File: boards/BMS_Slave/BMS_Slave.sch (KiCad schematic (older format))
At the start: 63 parts, among them J1 Mounting_Hole_4-40, J2 Mounting_Hole_4-40, J3 Mounting_Hole_4-40, J4 Mounting_Hole_4-40, J5 MicroFit_12, J6 MicroFit_20, J7 NanoFit_2, J8 NanoFit_2, Q1 Q_NPN_BCE, T1 T_LAN_7490100111A, U1 LTC6811-1, U2 24AA01, U3 MCP6001, U4 LTC1380, U5 LTC1380, U6 MCP6001

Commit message: Revert "testing"
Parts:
- J2, J4: footprint footprints:Mounting_Hole_Insert_4-40 -> footprints:Mounting_Hole_4-40
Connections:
- net CELL_TEMP1: now also J6.6; no longer J6.11
- net CELL_TEMP10: now also J6.16; no longer J6.20
- net CELL_TEMP2: now also J6.7; no longer J6.12
- net CELL_TEMP3: now also J6.8; no longer J6.13
- net CELL_TEMP4: now also J6.9; no longer J6.14
- net CELL_TEMP5: now also J6.10; no longer J6.15
- net CELL_TEMP6: now also J6.20; no longer J6.16
- net CELL_TEMP7: now also J6.19; no longer J6.17
- net CELL_TEMP9: now also J6.17; no longer J6.19
- net GND: now also J6.11, J6.12, J6.13, J6.14, J6.15; no longer J6.10, J6.6, J6.7, J6.8, J6.9
- net VREG: no longer U1.40 (ISOMD)
- net Cell1: no longer names the net of F10.1, J5.8
- net Cell10: no longer names the net of F1.1, J5.6
- net Cell2: no longer names the net of F9.1, J5.1
- net Cell3: no longer names the net of F8.1, J5.2
- net Cell4: no longer names the net of F7.1, J5.3
- net Cell5: no longer names the net of F6.1, J5.9
- net Cell6: no longer names the net of F5.1, J5.10
- net Cell7: no longer names the net of F4.1, J5.11
- net Cell8: no longer names the net of F3.1, J5.5
- net Cell9: no longer names the net of F2.1, J5.12
- net LowSide: no longer names the net of F11.1, J5.7
- net LowSide: no longer J5.4
- no-connect marks 15 -> 17
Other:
- moved on the sheet: J6

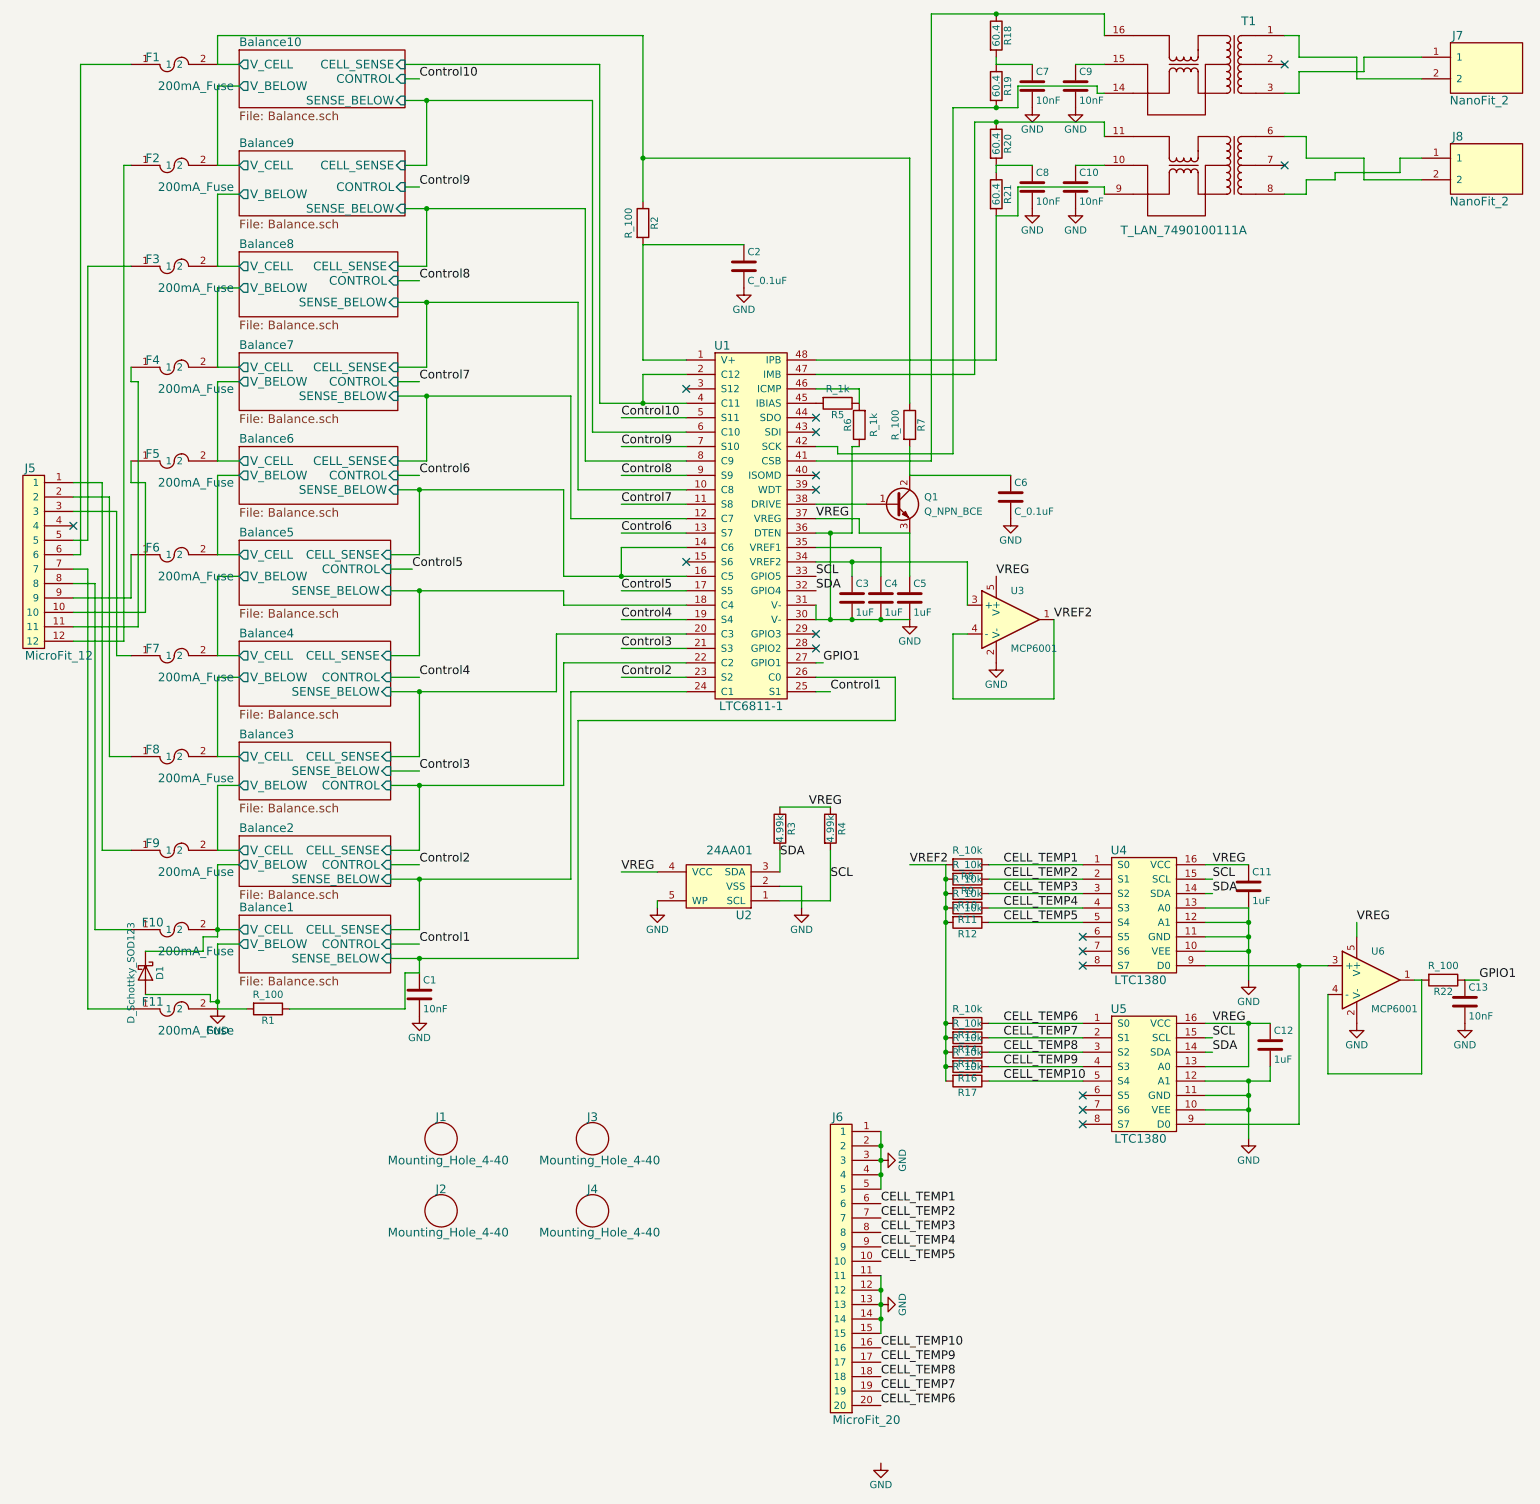
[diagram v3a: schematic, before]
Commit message: BMS Slave: Changed orientation of connectors
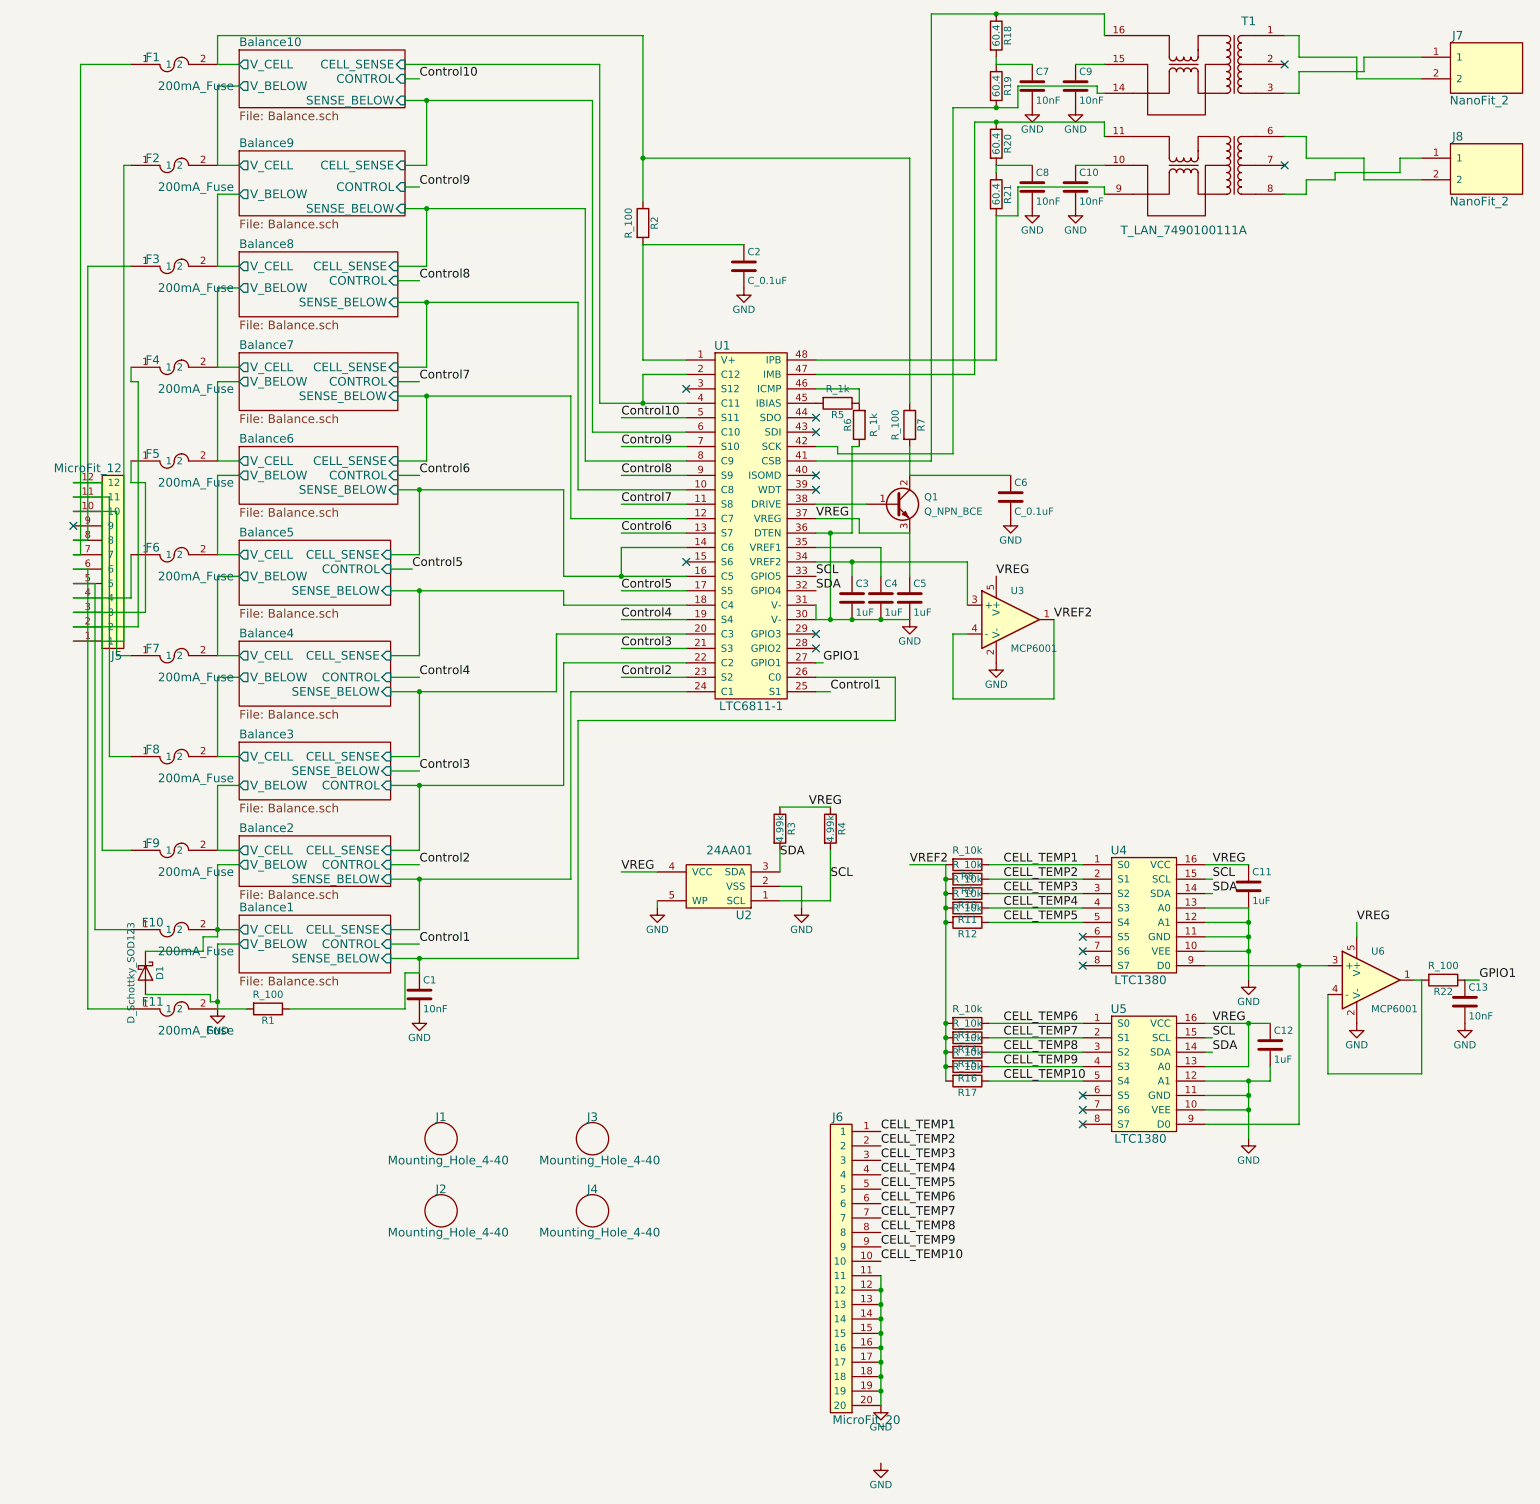
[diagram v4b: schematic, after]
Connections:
- net CELL_TEMP1: now also J6.1; no longer J6.6
- net CELL_TEMP10: now also J6.10; no longer J6.16
- net CELL_TEMP2: now also J6.2; no longer J6.7
- net CELL_TEMP3: now also J6.3; no longer J6.8
- net CELL_TEMP4: now also J6.4; no longer J6.9
- net CELL_TEMP5: now also J6.5; no longer J6.10
- net CELL_TEMP6: now also J6.6; no longer J6.20
- net CELL_TEMP7: now also J6.7; no longer J6.19
- net CELL_TEMP8: now also J6.8; no longer J6.18
- net CELL_TEMP9: now also J6.9; no longer J6.17
- net GND: now also J6.16, J6.17, J6.18, J6.19, J6.20; no longer J6.1, J6.2, J6.3, J6.4, J6.5
- net at F1.1: now also J5.7; no longer J5.6
- net at F2.1: now also J5.1; no longer J5.12
- net at F3.1: now also J5.8; no longer J5.5
- net at F4.1: now also J5.2; no longer J5.11
- net at F5.1: now also J5.3; no longer J5.10
- net at F6.1: now also J5.4; no longer J5.9
- net at F7.1: now also J5.10; no longer J5.3
- net at F8.1: now also J5.11; no longer J5.2
- net at F9.1: now also J5.12; no longer J5.1
- net at F10.1: now also J5.5; no longer J5.8
- net at F11.1: now also J5.6; no longer J5.7
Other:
- moved on the sheet: J5

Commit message: BMS Slave: Added CAD and updated Gerbers
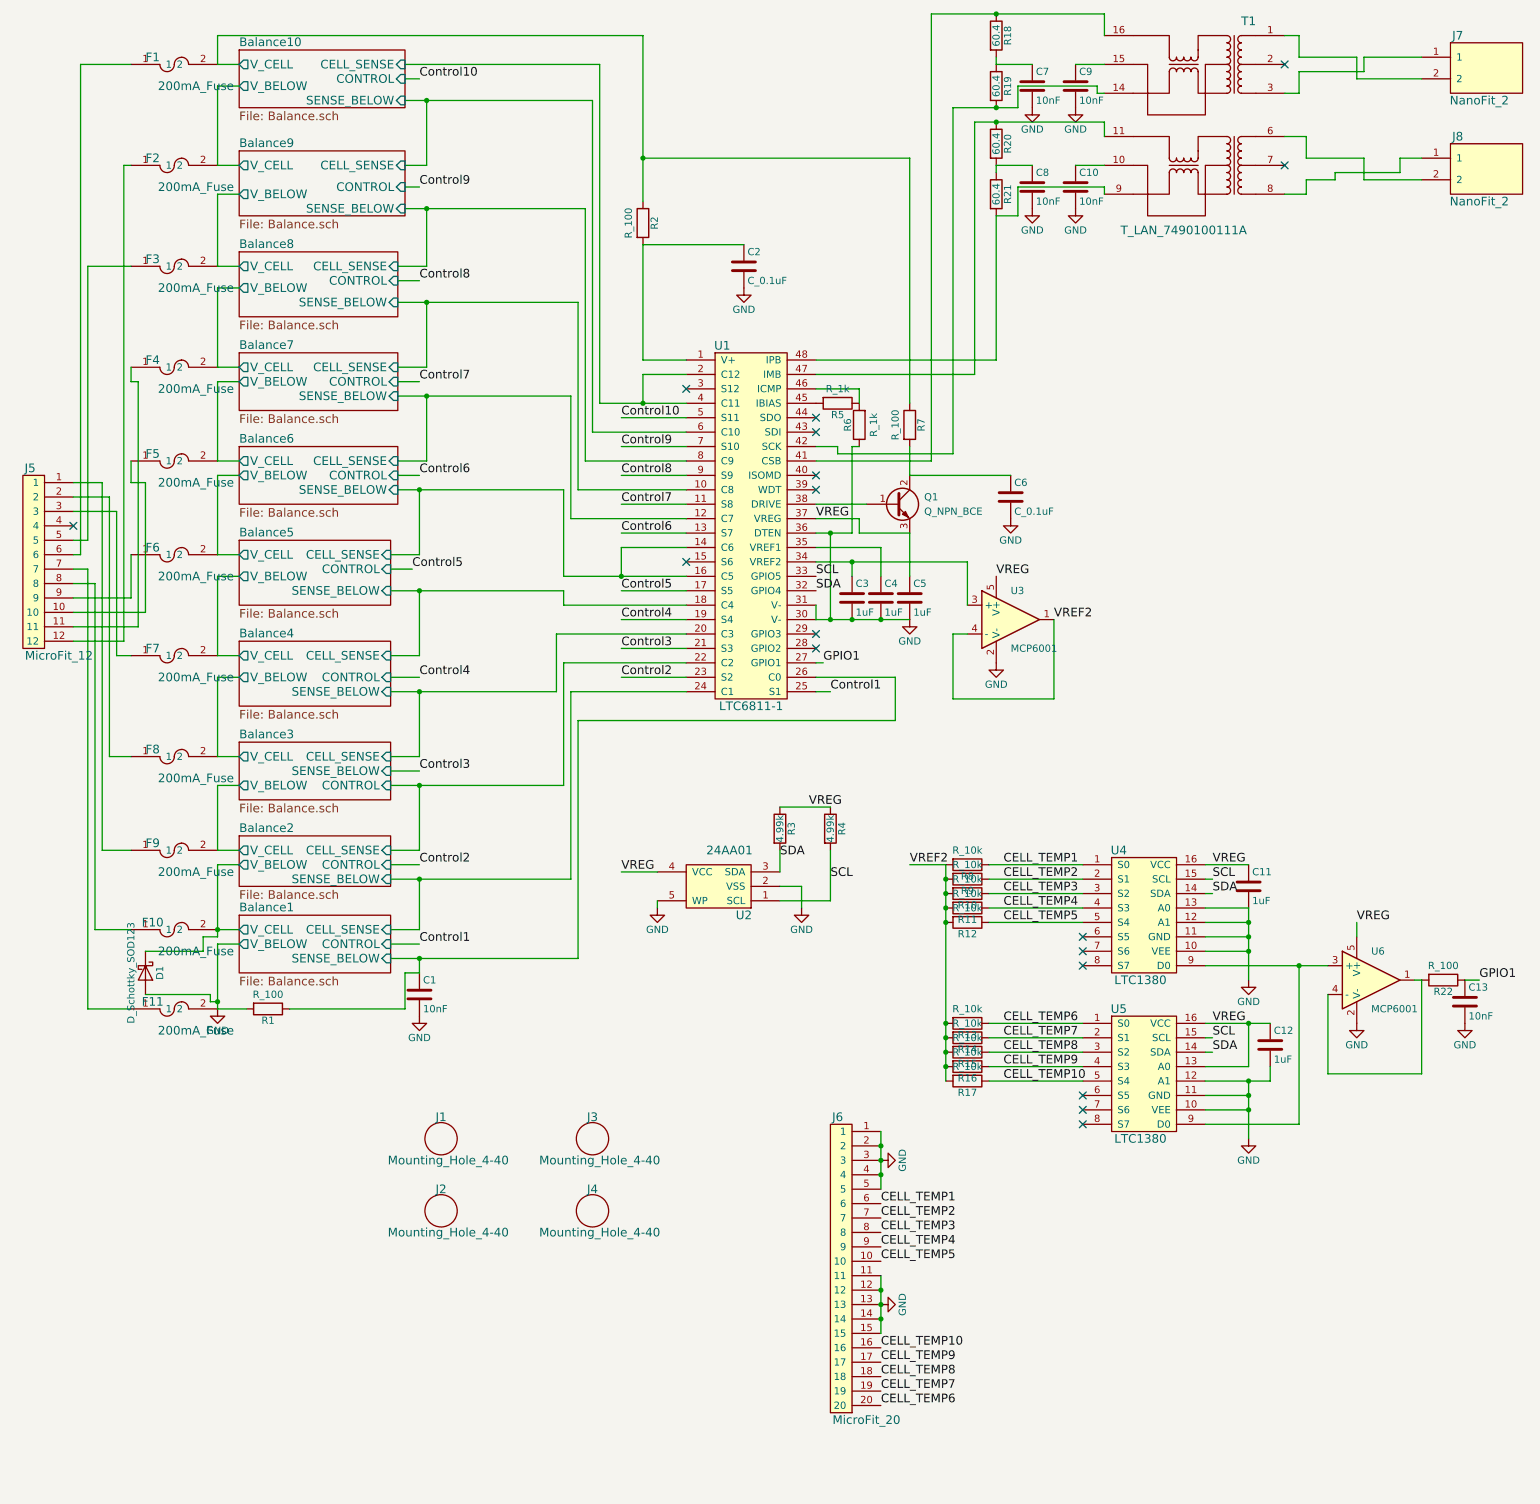
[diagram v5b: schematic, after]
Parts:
- J2, J4: footprint footprints:Mounting_Hole_4-40 -> footprints:Mounting_Hole_Insert_4-40
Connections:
- net CELL_TEMP1: now also J6.6; no longer J6.1
- net CELL_TEMP10: now also J6.16; no longer J6.10
- net CELL_TEMP2: now also J6.7; no longer J6.2
- net CELL_TEMP3: now also J6.8; no longer J6.3
- net CELL_TEMP4: now also J6.9; no longer J6.4
- net CELL_TEMP5: now also J6.10; no longer J6.5
- net CELL_TEMP6: now also J6.20; no longer J6.6
- net CELL_TEMP7: now also J6.19; no longer J6.7
- net CELL_TEMP8: now also J6.18; no longer J6.8
- net CELL_TEMP9: now also J6.17; no longer J6.9
- net GND: now also J6.1, J6.2, J6.3, J6.4, J6.5; no longer J6.16, J6.17, J6.18, J6.19, J6.20
- net at F1.1: now also J5.6; no longer J5.7
- net at F2.1: now also J5.12; no longer J5.1
- net at F3.1: now also J5.5; no longer J5.8
- net at F4.1: now also J5.11; no longer J5.2
- net at F5.1: now also J5.10; no longer J5.3
- net at F6.1: now also J5.9; no longer J5.4
- net at F7.1: now also J5.3; no longer J5.10
- net at F8.1: now also J5.2; no longer J5.11
- net at F9.1: now also J5.1; no longer J5.12
- net at F10.1: now also J5.8; no longer J5.5
- net at F11.1: now also J5.7; no longer J5.6
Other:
- moved on the sheet: J5
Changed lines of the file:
@@
 F 0 "J4" H 4400 9050 60  0000 C CNN
 F 1 "Mounting_Hole_4-40" H 4450 8750 60  0000 C CNN
-F 2 "footprints:Mounting_Hole_4-40" H 4300 8950 60  0001 C CNN
+F 2 "footprints:Mounting_Hole_Insert_4-40" H 4300 8950 60  0001 C CNN
 F 3 "" H 4400 8900 60  0001 C CNN
 F 4 "Value" H 4400 8900 60  0001 C CNN "MFN"
@@
 F 0 "J2" H 3350 9050 60  0000 C CNN
 F 1 "Mounting_Hole_4-40" H 3400 8750 60  0000 C CNN
-F 2 "footprints:Mounting_Hole_4-40" H 3250 8950 60  0001 C CNN
+F 2 "footprints:Mounting_Hole_Insert_4-40" H 3250 8950 60  0001 C CNN
 F 3 "" H 3350 8900 60  0001 C CNN
 F 4 "Value" H 3350 8900 60  0001 C CNN "MFN"
@@
 	1    0    0    -1
 $EndComp
-Text Label 6400 8350 0    60   ~ 0
+Text Label 6400 8850 0    60   ~ 0
 CELL_TEMP1
-Text Label 6400 8450 0    60   ~ 0
+Text Label 6400 8950 0    60   ~ 0
 CELL_TEMP2
-Text Label 6400 8550 0    60   ~ 0
+Text Label 6400 9050 0    60   ~ 0
 CELL_TEMP3
-Text Label 6400 8650 0    60   ~ 0
+Text Label 6400 9150 0    60   ~ 0
 CELL_TEMP4
-Text Label 6400 8750 0    60   ~ 0
+Text Label 6400 9250 0    60   ~ 0
 CELL_TEMP5
-Text Label 6400 8850 0    60   ~ 0
+Text Label 6400 10250 0    60   ~ 0
 CELL_TEMP6
-Text Label 6400 8950 0    60   ~ 0
+Text Label 6400 10150 0    60   ~ 0
 CELL_TEMP7
-Text Label 6400 9050 0    60   ~ 0
+Text Label 6400 10050 0    60   ~ 0
 CELL_TEMP8
-Text Label 6400 9150 0    60   ~ 0
+Text Label 6400 9950 0    60   ~ 0
 CELL_TEMP9
-Text Label 6400 9250 0    60   ~ 0
+Text Label 6400 9850 0    60   ~ 0
 CELL_TEMP10
-$Comp
-L GND #PWR017
-U 1 1 5A00BA8F
-P 6400 10650
-F 0 "#PWR017" H 6400 10400 50  0001 C CNN
-F 1 "GND" H 6400 10500 50  0000 C CNN
-F 2 "" H 6400 10650 50  0001 C CNN
-F 3 "" H 6400 10650 50  0001 C CNN
-	1    6400 10650
-	1    0    0    -1
-$EndComp
 NoConn ~ 9200 950
 NoConn ~ 9200 1650
@@
 L MicroFit_12 J5
 U 1 1 5A1DBB3E
-P 1350 5150
-F 0 "J5" H 1600 5050 60  0000 C CNN
-F 1 "MicroFit_12" H 1800 3750 60  0000 C CNN
-F 2 "footprints:Microfit3_Header_02x06_Angled_OEM" H 1350 5150 60  0001 C CNN
-F 3 "" H 1350 5150 60  0001 C CNN
-	1    1350 5150
-	-1   0    0    1
+P 250 3650
+F 0 "J5" H 500 3550 60  0000 C CNN
+F 1 "MicroFit_12" H 700 2250 60  0000 C CNN
+F 2 "footprints:Microfit3_Header_02x06_Angled_OEM" H 250 3650 60  0001 C CNN
+F 3 "" H 250 3650 60  0001 C CNN
+	1    250  3650
+	1    0    0    -1
+$EndComp
+NoConn ~ 800  4150
+$Comp
+L GND #PWR017
+U 1 1 5A00BA8F
+P 6400 9550
+F 0 "#PWR017" H 6400 9300 50  0001 C CNN
+F 1 "GND" H 6400 9400 50  0000 C CNN
+F 2 "" H 6400 9550 50  0001 C CNN
+F 3 "" H 6400 9550 50  0001 C CNN
+	1    6400 9550
+	0    -1   -1   0
 $EndComp
 $Comp
 L GND #PWR018
 U 1 1 5A59223B
-P 6400 10250
-F 0 "#PWR018" H 6400 10000 50  0001 C CNN
-F 1 "GND" H 6400 10100 50  0000 C CNN
-F 2 "" H 6400 10250 50  0001 C CNN
-F 3 "" H 6400 10250 50  0001 C CNN
-	1    6400 10250
-	1    0    0    -1
-$EndComp
-NoConn ~ 800  4150
+P 6400 8550
+F 0 "#PWR018" H 6400 8300 50  0001 C CNN
+F 1 "GND" H 6400 8400 50  0000 C CNN
+F 2 "" H 6400 8550 50  0001 C CNN
+F 3 "" H 6400 8550 50  0001 C CNN
+	1    6400 8550
+	0    -1   -1   0
+$EndComp
 $Comp
 L MicroFit_20 J6
@@
 	1    0    0    -1
 $EndComp
-Connection ~ 6400 10150
-Connection ~ 6400 10050
-Connection ~ 6400 9950
-Connection ~ 6400 9850
-Connection ~ 6400 9750
-Connection ~ 6400 9650
-Connection ~ 6400 9550
-Connection ~ 6400 9450
-Wire Wire Line
-	6400 9350 6400 10250
 Wire Wire Line
 	1200 4650 800  4650
@@
 	7350 2000 7200 2000
 Wire Wire Line
-	7350 1100 7350 1250
-Wire Wire Line
-	7900 1100 7350 1100
-Wire Wire Line
-	7900 1150 7900 1100
-Wire Wire Line
-	7950 1150 7900 1150
+	7350 1250 7350 1100
+Wire Wire Line
+	7350 1100 7900 1100
+Wire Wire Line
+	7900 1100 7900 1150
+Wire Wire Line
+	7900 1150 7950 1150
 Wire Wire Line
 	7950 950  7750 950
@@
 Wire Wire Line
 	1800 750  4750 750
+Wire Wire Line
+	6400 8350 6400 8750
+Connection ~ 6400 8450
+Connection ~ 6400 8550
+Connection ~ 6400 8650
+Wire Wire Line
+	6400 9350 6400 9750
+Connection ~ 6400 9450
+Connection ~ 6400 9550
+Connection ~ 6400 9650
 $EndSCHEMATC
